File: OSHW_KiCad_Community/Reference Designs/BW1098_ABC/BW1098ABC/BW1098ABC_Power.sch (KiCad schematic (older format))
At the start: 32 parts

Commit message: all footprints associated on bw1098abc board except two I need to clarify with Brian. Need to talk to chris about power
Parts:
- C? (x10): footprint Capacitor_SMD:C_0201_0603Metric -> Capacitor_SMD:C_0603_1608Metric
- L?: footprint (none) -> OSHW_LuxonisMaster_20201223:DFE252012P-1R0M=P2
- R? (x2): footprint Resistor_SMD:R_0402_1005Metric -> Resistor_SMD:R_0603_1608Metric
- U? (x3): footprint (none) -> digikey-footprints:SC-70-5
- U?: footprint (none) -> Package_SON:WSON-8-1EP_2x2mm_P0.5mm_EP0.9x1.6mm
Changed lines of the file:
@@
 F 0 "C?" V 4860 1910 60  0000 R TNN
 F 1 "22uF 0603" V 4760 1910 60  0000 R TNN
-F 2 "Capacitor_SMD:C_0201_0603Metric" H 4760 1910 60  0001 C CNN
+F 2 "Capacitor_SMD:C_0603_1608Metric" H 4760 1910 60  0001 C CNN
 F 3 "" H 4760 1910 60  0000 C CNN
 F 4 "10V" V -650 2400 60  0001 C CNN "Voltage Rating"
@@
 F 0 "C?" V 4960 9860 60  0000 R TNN
 F 1 "22uF 0603" V 4860 9860 60  0000 R TNN
-F 2 "Capacitor_SMD:C_0201_0603Metric" H 4860 9860 60  0001 C CNN
+F 2 "Capacitor_SMD:C_0603_1608Metric" H 4860 9860 60  0001 C CNN
 F 3 "" H 4860 9860 60  0000 C CNN
 F 4 "10V" V -650 2000 60  0001 C CNN "Voltage Rating"
@@
 F 0 "C?" V 1910 6510 60  0000 R TNN
 F 1 "10uF 0603" V 1810 6510 60  0000 R TNN
-F 2 "Capacitor_SMD:C_0201_0603Metric" H 1810 6510 60  0001 C CNN
+F 2 "Capacitor_SMD:C_0603_1608Metric" H 1810 6510 60  0001 C CNN
 F 3 "" H 1810 6510 60  0000 C CNN
 F 4 "10V" V -650 2000 60  0001 C CNN "Voltage Rating"
@@
 F 0 "C?" V 1910 7610 60  0000 R TNN
 F 1 "10uF 0603" V 1810 7610 60  0000 R TNN
-F 2 "Capacitor_SMD:C_0201_0603Metric" H 1810 7610 60  0001 C CNN
+F 2 "Capacitor_SMD:C_0603_1608Metric" H 1810 7610 60  0001 C CNN
 F 3 "" H 1810 7610 60  0000 C CNN
 F 4 "10V" V -650 2000 60  0001 C CNN "Voltage Rating"
@@
 F 0 "C?" V 1310 8610 60  0000 R TNN
 F 1 "10uF 0603" V 1210 8610 60  0000 R TNN
-F 2 "Capacitor_SMD:C_0201_0603Metric" H 1210 8610 60  0001 C CNN
+F 2 "Capacitor_SMD:C_0603_1608Metric" H 1210 8610 60  0001 C CNN
 F 3 "" H 1210 8610 60  0000 C CNN
 F 4 "10V" V -650 2000 60  0001 C CNN "Voltage Rating"
@@
 F 0 "C?" V 3810 6510 60  0000 R TNN
 F 1 "10uF 0603" V 3710 6510 60  0000 R TNN
-F 2 "Capacitor_SMD:C_0201_0603Metric" H 3710 6510 60  0001 C CNN
+F 2 "Capacitor_SMD:C_0603_1608Metric" H 3710 6510 60  0001 C CNN
 F 3 "" H 3710 6510 60  0000 C CNN
 F 4 "10V" V -650 2000 60  0001 C CNN "Voltage Rating"
@@
 F 0 "C?" V 3810 7610 60  0000 R TNN
 F 1 "10uF 0603" V 3710 7610 60  0000 R TNN
-F 2 "Capacitor_SMD:C_0201_0603Metric" H 3710 7610 60  0001 C CNN
+F 2 "Capacitor_SMD:C_0603_1608Metric" H 3710 7610 60  0001 C CNN
 F 3 "" H 3710 7610 60  0000 C CNN
 F 4 "10V" V -650 2000 60  0001 C CNN "Voltage Rating"
@@
 F 0 "L?" H 4150 8800 60  0000 L BNN
 F 1 "1uH, 3.2A, 20%" H 4050 8650 60  0000 L BNN
-F 2 "" H 4050 8650 60  0001 C CNN
+F 2 "OSHW_LuxonisMaster_20201223:DFE252012P-1R0M=P2" H 4050 8650 60  0001 C CNN
 F 3 "" H 4050 8650 60  0000 C CNN
 	1    4050 8750
@@
 F 0 "C?" V 3810 5460 60  0000 R TNN
 F 1 "10uF 0603" V 3710 5460 60  0000 R TNN
-F 2 "Capacitor_SMD:C_0201_0603Metric" H 3710 5460 60  0001 C CNN
+F 2 "Capacitor_SMD:C_0603_1608Metric" H 3710 5460 60  0001 C CNN
 F 3 "" H 3710 5460 60  0000 C CNN
 F 4 "10V" V -650 2000 60  0001 C CNN "Voltage Rating"
@@
 F 0 "C?" V 1910 5460 60  0000 R TNN
 F 1 "10uF 0603" V 1810 5460 60  0000 R TNN
-F 2 "Capacitor_SMD:C_0201_0603Metric" H 1810 5460 60  0001 C CNN
+F 2 "Capacitor_SMD:C_0603_1608Metric" H 1810 5460 60  0001 C CNN
 F 3 "" H 1810 5460 60  0000 C CNN
 F 4 "10V" V -650 2000 60  0001 C CNN "Voltage Rating"
@@
 F 0 "U?" H 2600 5350 60  0000 L BNN
 F 1 "TLV70012DCK" H 2600 4850 60  0000 L BNN
-F 2 "" H 2600 4850 60  0001 C CNN
+F 2 "digikey-footprints:SC-70-5" H 2600 4850 60  0001 C CNN
 F 3 "" H 2600 4850 60  0000 C CNN
 	1    2400 5250
@@
 F 0 "U?" H 2600 7500 60  0000 L BNN
 F 1 "TLV70028DCK" H 2600 7000 60  0000 L BNN
-F 2 "" H 2600 7000 60  0001 C CNN
+F 2 "digikey-footprints:SC-70-5" H 2600 7000 60  0001 C CNN
 F 3 "" H 2600 7000 60  0000 C CNN
 	1    2400 7400
@@
 F 0 "U?" H 2600 6400 60  0000 L BNN
 F 1 "TLV70018DCK" H 2600 5900 60  0000 L BNN
-F 2 "" H 2600 5900 60  0001 C CNN
+F 2 "digikey-footprints:SC-70-5" H 2600 5900 60  0001 C CNN
 F 3 "" H 2600 5900 60  0000 C CNN
 	1    2400 6300
@@
 F 0 "U?" H 2400 8750 60  0000 L BNN
 F 1 "TLV62080DSG" H 3100 7650 60  0000 L BNN
-F 2 "" H 3100 7650 60  0001 C CNN
+F 2 "Package_SON:WSON-8-1EP_2x2mm_P0.5mm_EP0.9x1.6mm" H 3100 7650 60  0001 C CNN
 F 3 "" H 3100 7650 60  0000 C CNN
 	1    2200 8550
@@
 F 0 "R?" H 2740 1530 60  0000 L BNN
 F 1 "0R 0603" H 2740 1370 60  0000 L BNN
-F 2 "Resistor_SMD:R_0402_1005Metric" H 2740 1370 60  0001 C CNN
+F 2 "Resistor_SMD:R_0603_1608Metric" H 2740 1370 60  0001 C CNN
 F 3 "" H 2740 1370 60  0000 C CNN
 	1    2650 1500
@@
 F 0 "R?" H 2790 3730 60  0000 L BNN
 F 1 "0R 0603" H 2790 3570 60  0000 L BNN
-F 2 "Resistor_SMD:R_0402_1005Metric" H 2790 3570 60  0001 C CNN
+F 2 "Resistor_SMD:R_0603_1608Metric" H 2790 3570 60  0001 C CNN
 F 3 "" H 2790 3570 60  0000 C CNN
 	1    2700 3700
@@
 F 0 "C?" V 4110 1910 60  0000 R TNN
 F 1 "22uF 0603" V 4050 2000 60  0000 R TNN
-F 2 "Capacitor_SMD:C_0201_0603Metric" H 4010 1910 60  0001 C CNN
+F 2 "Capacitor_SMD:C_0603_1608Metric" H 4010 1910 60  0001 C CNN
 F 3 "" H 4010 1910 60  0000 C CNN
 F 4 "10V" V -650 2400 60  0001 C CNN "Voltage Rating"

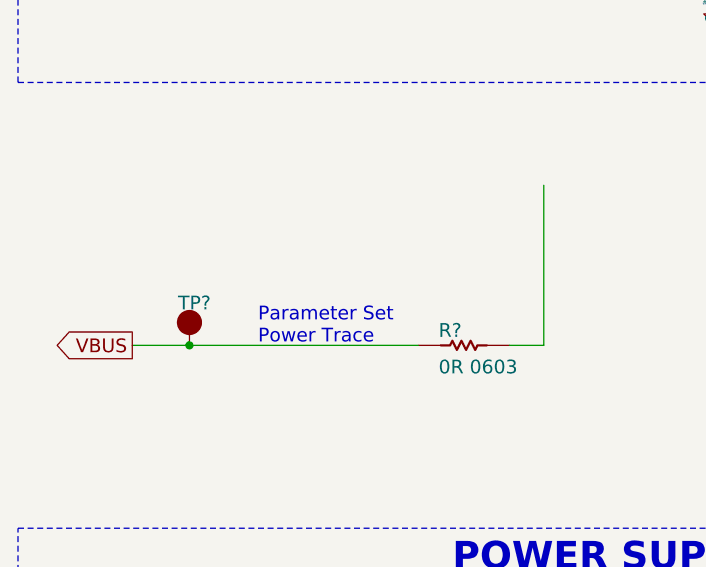
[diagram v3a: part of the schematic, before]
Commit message: added datasheets for everything but resistors caps and inductors
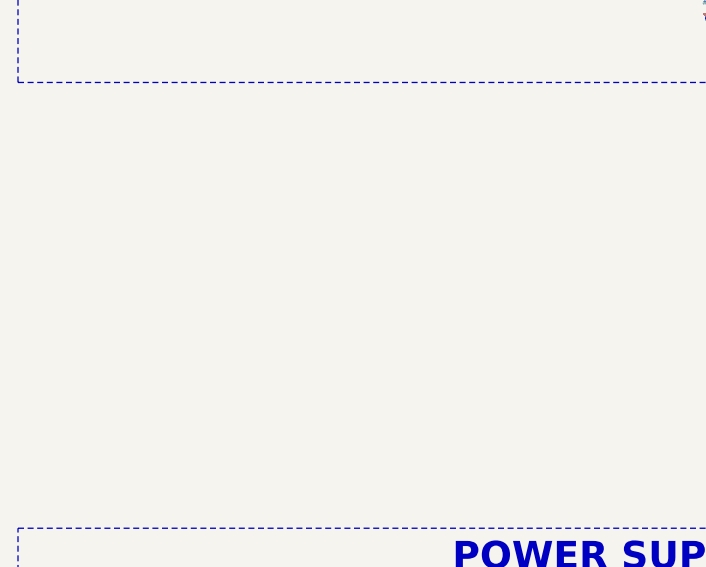
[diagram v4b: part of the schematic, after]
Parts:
- removed R?: 0R 0603, Resistor_SMD:R_0603_1608Metric, symbol BW1098ABC-rescue:CRCW06030000Z0EA-depthAI_sch
- removed TP?: TEST_POINT, TestPoint:TestPoint_Loop_D1.80mm_Drill1.0mm_Beaded, symbol BW1098ABC-rescue:TEST_POINT-depthAI_sch
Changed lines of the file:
@@
 	2050 8150 1200 8150
-Wire Wire Line
-	3250 3700 3250 3000
-Wire Wire Line
-	3100 3700 3250 3700
 Wire Wire Line
 	1950 1700 1700 1700
@@
 F 1 "TLV70012DCK" H 2600 4850 60  0000 L BNN
 F 2 "digikey-footprints:SC-70-5" H 2600 4850 60  0001 C CNN
-F 3 "" H 2600 4850 60  0000 C CNN
+F 3 "https://www.ti.com/lit/ds/symlink/tlv700.pdf?ts=1610324804784&ref_url=https%253A%252F%252Fwww.ti.com%252Fproduct%252FTLV700" H 2600 4850 60  0001 C CNN
 	1    2400 5250
 	1    0    0    -1
@@
 F 1 "TLV70028DCK" H 2600 7000 60  0000 L BNN
 F 2 "digikey-footprints:SC-70-5" H 2600 7000 60  0001 C CNN
-F 3 "" H 2600 7000 60  0000 C CNN
+F 3 "https://www.ti.com/lit/ds/symlink/tlv700.pdf?ts=1610324804784&ref_url=https%253A%252F%252Fwww.ti.com%252Fproduct%252FTLV700" H 2600 7000 60  0001 C CNN
 	1    2400 7400
 	1    0    0    -1
@@
 $EndComp
 $Comp
-L BW1098ABC-rescue:TEST_POINT-depthAI_sch TP?
-U 1 1 604BD5AB
-P 1700 3700
-AR Path="/5FD7EFCB/604BD5AB" Ref="TP?"  Part="1"
-AR Path="/604AEAFA/604BD5AB" Ref="TP?"  Part="1"
-F 0 "TP?" H 1650 3850 60  0000 L BNN
-F 1 "TEST_POINT" H 1700 3700 50  0001 C CNN
-F 2 "TestPoint:TestPoint_Loop_D1.80mm_Drill1.0mm_Beaded" H 1700 3700 50  0001 C CNN
-F 3 "" H 1700 3700 50  0001 C CNN
-	1    1700 3700
-	1    0    0    -1
-$EndComp
-$Comp
 L BW1098ABC-rescue:TLV70018DCK-depthAI_sch U?
 U 1 1 604BD5B1
@@
 F 1 "TLV70018DCK" H 2600 5900 60  0000 L BNN
 F 2 "digikey-footprints:SC-70-5" H 2600 5900 60  0001 C CNN
-F 3 "" H 2600 5900 60  0000 C CNN
+F 3 "https://www.ti.com/lit/ds/symlink/tlv700.pdf?ts=1610324804784&ref_url=https%253A%252F%252Fwww.ti.com%252Fproduct%252FTLV700" H 2600 5900 60  0001 C CNN
 	1    2400 6300
 	1    0    0    -1
@@
 F 1 "TLV62080DSG" H 3100 7650 60  0000 L BNN
 F 2 "Package_SON:WSON-8-1EP_2x2mm_P0.5mm_EP0.9x1.6mm" H 3100 7650 60  0001 C CNN
-F 3 "" H 3100 7650 60  0000 C CNN
+F 3 "https://www.ti.com/lit/ds/symlink/tlv62080.pdf?ts=1610324868570&ref_url=https%253A%252F%252Fwww.ti.com%252Fproduct%252FTLV62080" H 3100 7650 60  0001 C CNN
 	1    2200 8550
 	1    0    0    -1
@@
 F 1 "B2B-PH-K-S(LF)(SN)" H 14400 7350 60  0000 L BNN
 F 2 "OSHW_LuxonisMaster_20201223:B2B-PH-K-S(LF)(SN)" H 14400 7350 60  0001 C CNN
-F 3 "" H 14400 7350 60  0000 C CNN
+F 3 "http://www.jst-mfg.com/product/pdf/eng/ePH.pdf" H 14400 7350 60  0001 C CNN
 	1    14100 7750
 	1    0    0    -1
@@
 F 3 "" H 2740 1370 60  0000 C CNN
 	1    2650 1500
-	1    0    0    -1
-$EndComp
-$Comp
-L BW1098ABC-rescue:CRCW06030000Z0EA-depthAI_sch R?
-U 1 1 604BD5C9
-P 2700 3700
-AR Path="/5FD7EFCB/604BD5C9" Ref="R?"  Part="1"
-AR Path="/604AEAFA/604BD5C9" Ref="R?"  Part="1"
-F 0 "R?" H 2790 3730 60  0000 L BNN
-F 1 "0R 0603" H 2790 3570 60  0000 L BNN
-F 2 "Resistor_SMD:R_0603_1608Metric" H 2790 3570 60  0001 C CNN
-F 3 "" H 2790 3570 60  0000 C CNN
-	1    2700 3700
 	1    0    0    -1
 $EndComp
@@
 Wire Wire Line
 	1600 7400 1800 7400
-Wire Wire Line
-	1450 3700 1700 3700
 Wire Wire Line
 	1550 6300 1800 6300
@@
 Text GLabel 6050 8750 2    60   Output ~ 0
 1V05
-Text GLabel 1450 3700 0    60   Output ~ 0
-VBUS
 Text GLabel 6100 1500 3    60   Output ~ 0
 VDD_5V
@@
 Text Notes 5150 1500 0    60   ~ 0
 Parameter Set\nPower Trace
-Text Notes 2000 3700 0    60   ~ 0
-Parameter Set\nPower Trace
 Text GLabel 5950 5250 3    60   Output ~ 0
 1V2
 Text GLabel 1500 5250 0    60   Input ~ 0
 VDD_5V
-Connection ~ 1700 3700
-Wire Wire Line
-	1700 3700 2700 3700
 Connection ~ 1800 5250
 Wire Wire Line

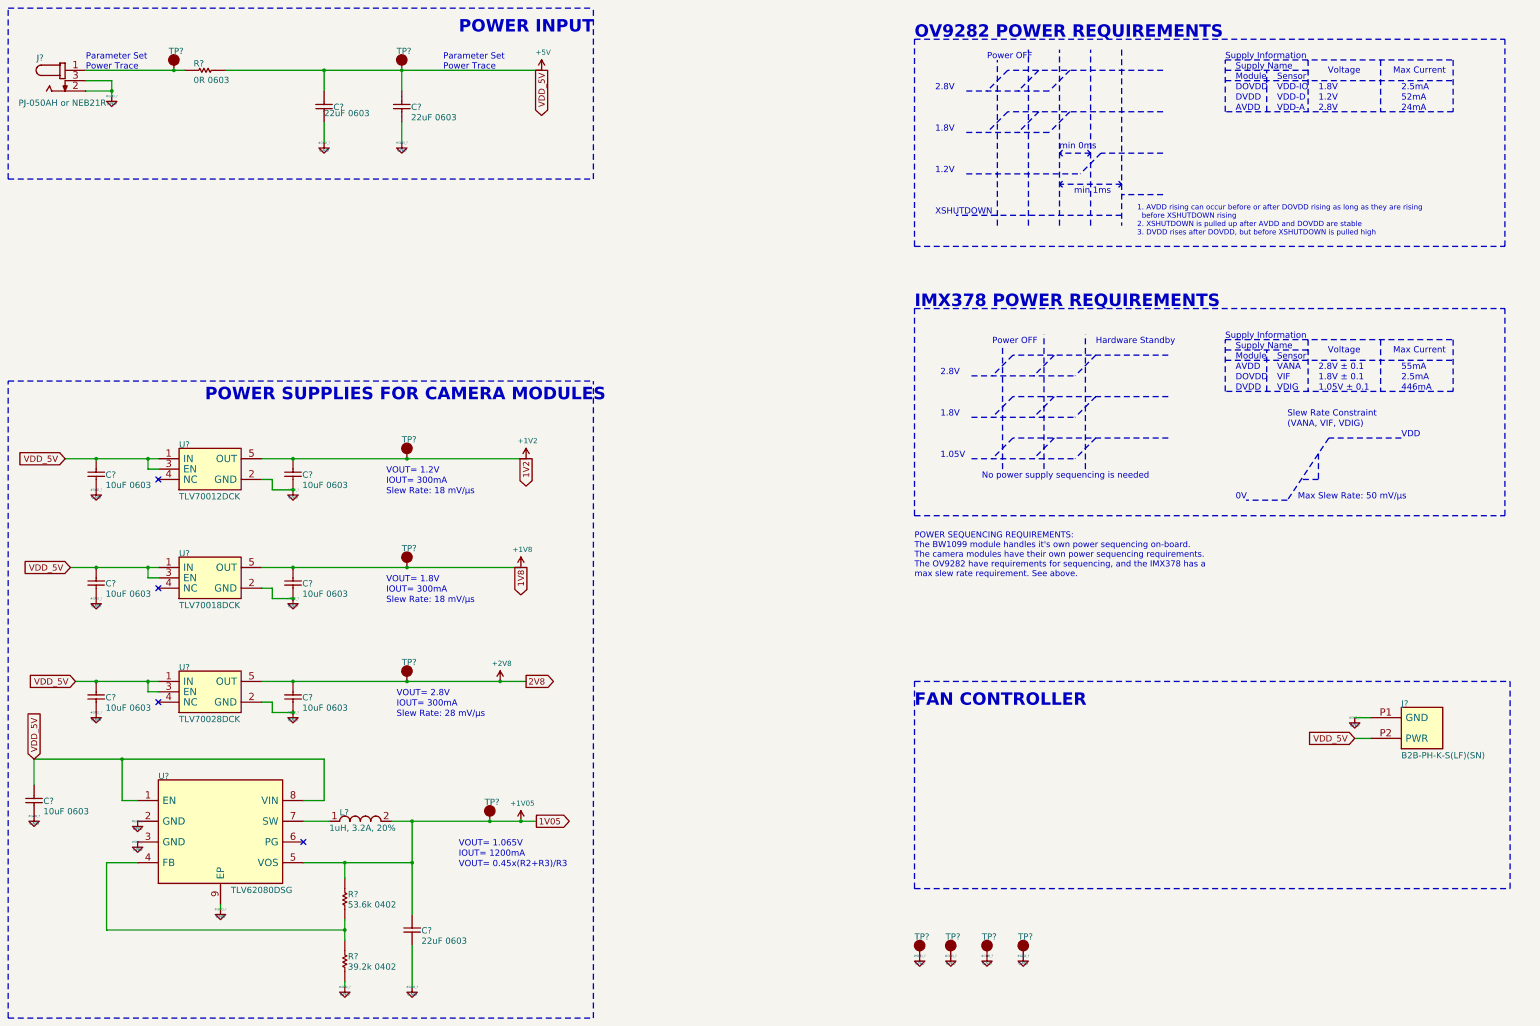
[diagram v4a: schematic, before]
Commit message: added busses, fixed hierarchical labeling, just need to fix an erc thing with my buses then itll pass
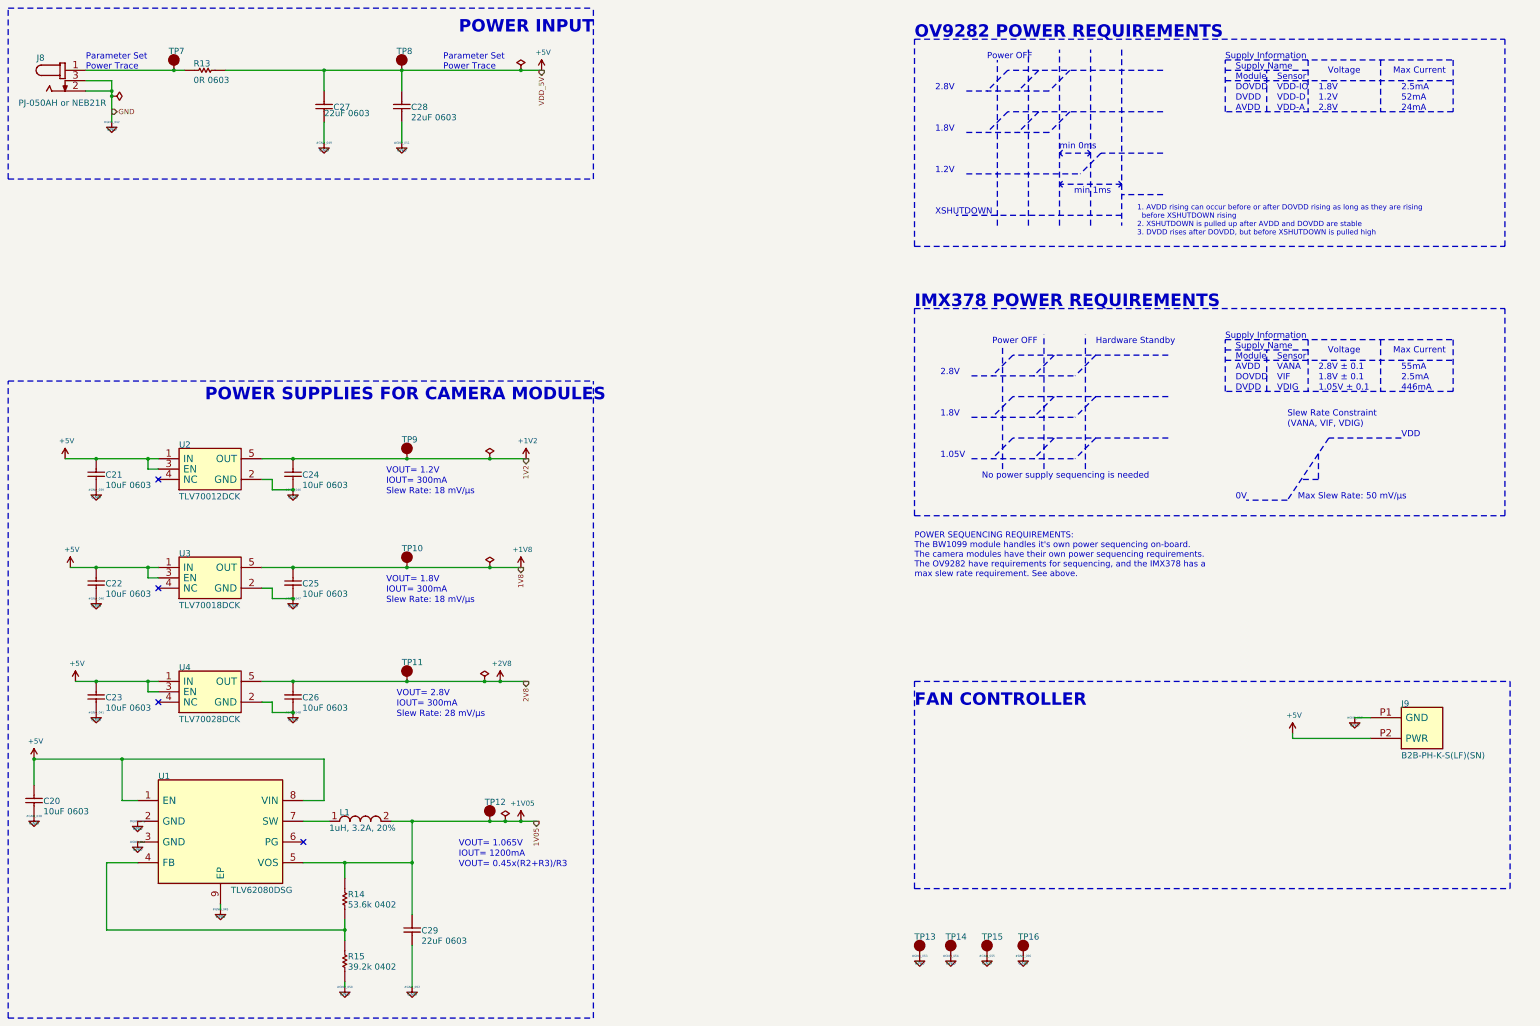
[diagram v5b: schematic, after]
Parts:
- gave numbers to parts that had none: 30
